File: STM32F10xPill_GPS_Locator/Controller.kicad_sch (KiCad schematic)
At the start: 0 parts

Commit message: Add controller and clocks
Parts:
- added C1, C2, C3, C4: 20p, symbol Device:C
- added R1: 1M, symbol Device:R_US
- added U1: STM32F100C4Tx, Package_QFP:LQFP-48_7x7mm_P0.5mm, symbol MCU_ST_STM32F1:STM32F100C4Tx
- added U2: ~, symbol Utilities:Net_Tie
- added Y1: 16MHz, symbol Device:Crystal
- added Y2: 32.768kHz, symbol Device:Crystal
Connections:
- new net: U1.23 (VSS), U1.35 (VSS), U1.47 (VSS)
- new net: C3.2, U1.3 (PC14), Y2.2
- new net: C4.2, U1.4 (PC15), Y2.1
- new net GND: C3.1, C4.1
- new net MCU_OSCIN: C1.2, R1.1, U1.5 (PD0), Y1.2
- new net MCU_OSCOUT: C2.2, R1.2, U1.6 (PD1), Y1.1
- new net MCU_OSC_COM: C1.1, C2.1
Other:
- company: (none) -> MTP
- title: (none) -> STM32F100C4T6B GPS Locator

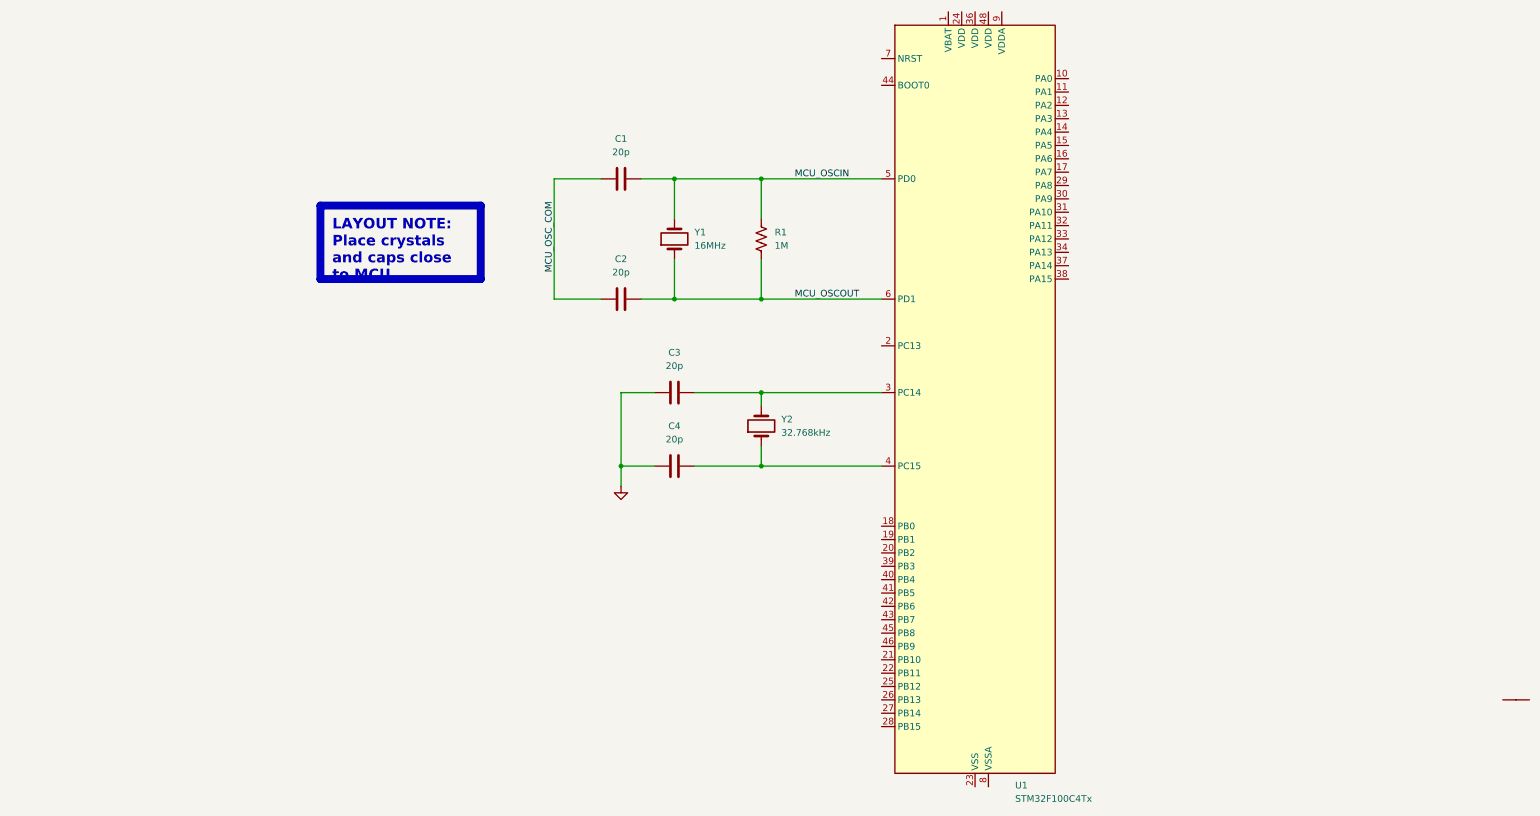
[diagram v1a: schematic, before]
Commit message: Tuned oscillator components
Made more accurate according to the device datasheet as well as AN2867
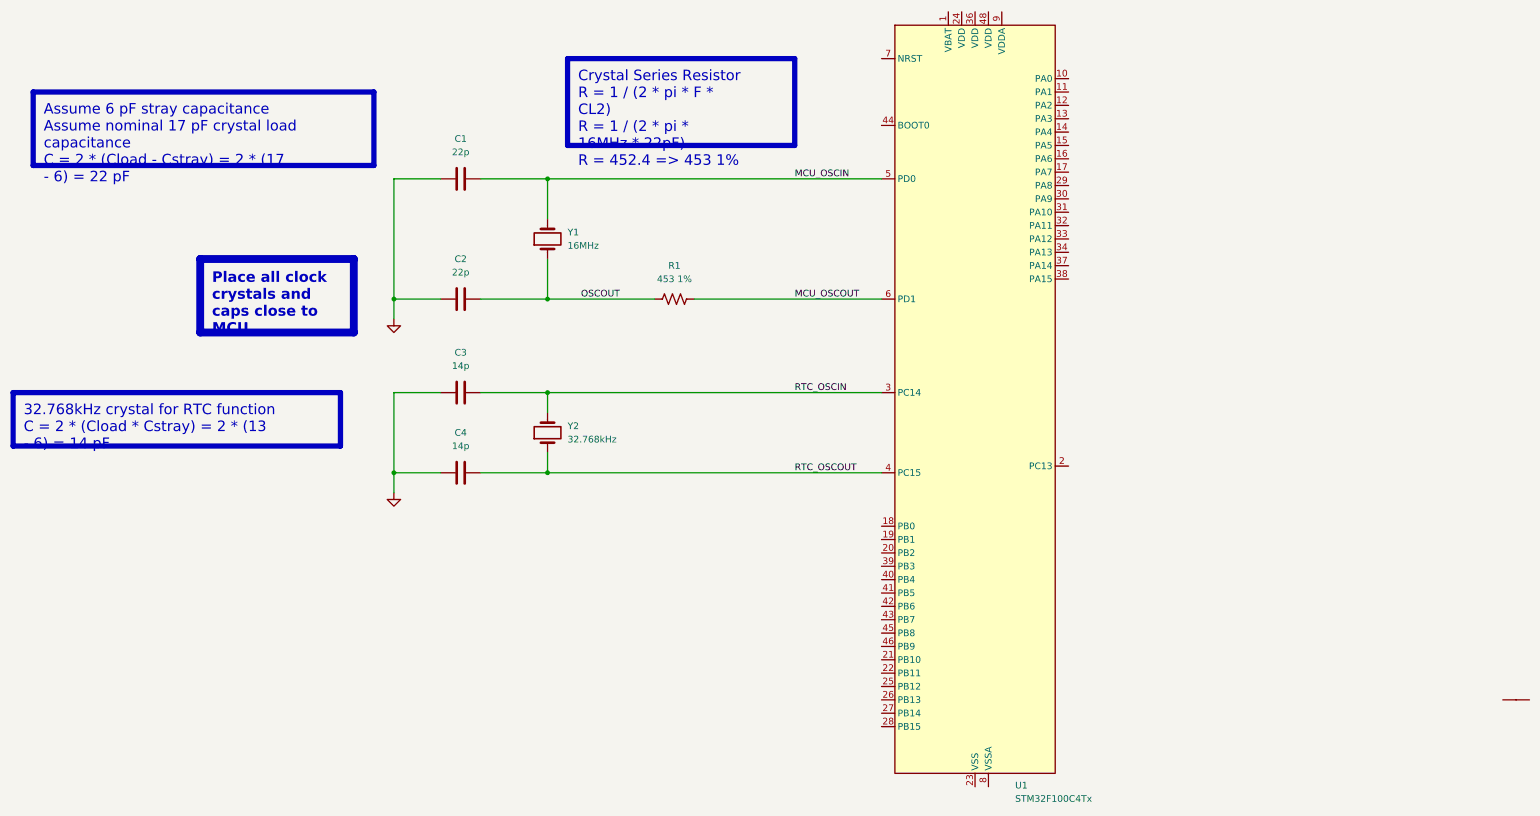
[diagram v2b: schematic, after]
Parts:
- C1, C2: value 20p -> 22p
- C3, C4: value 20p -> 14p
- R1: value 1M -> 453 1%
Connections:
- net MCU_OSC_COM is gone; now on net GND: C1.1, C2.1
- net MCU_OSCIN: no longer R1.1
- net MCU_OSCOUT: no longer C2.2, Y1.1
- net RTC_OSCIN: now reaches C3.2, U1.3 (PC14), Y2.2
- net RTC_OSCOUT: now reaches C4.2, U1.4 (PC15), Y2.1
- new net OSCOUT: C2.2, R1.1, Y1.1
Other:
- moved on the sheet: C1, C2, C3, C4, R1, Y1, Y2
